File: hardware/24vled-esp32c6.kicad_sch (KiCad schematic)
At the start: 19 parts, among them J1 2601-1106, J3 Barrel_Jack, Q1 AO3400A, Q2 AO3400A, Q3 AO3400A, Q4 AO3400A, Q5 AO3400A, U1 R-78E5.0-1.0

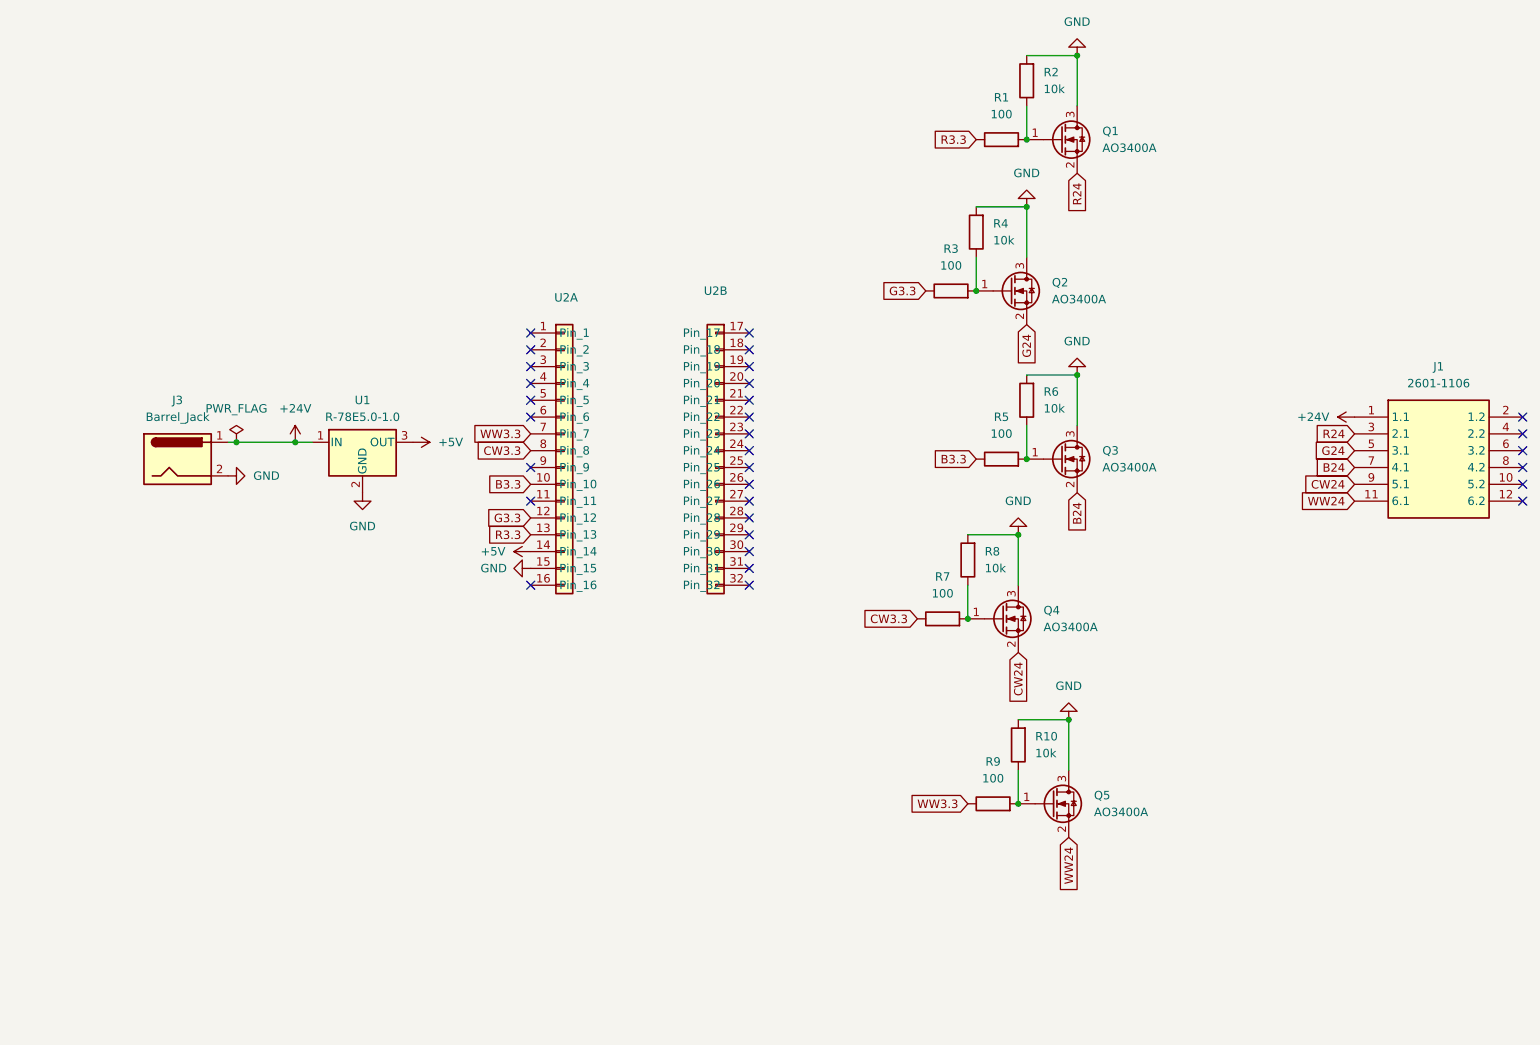
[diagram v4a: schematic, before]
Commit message: add the large cap and remove the flyback diodes
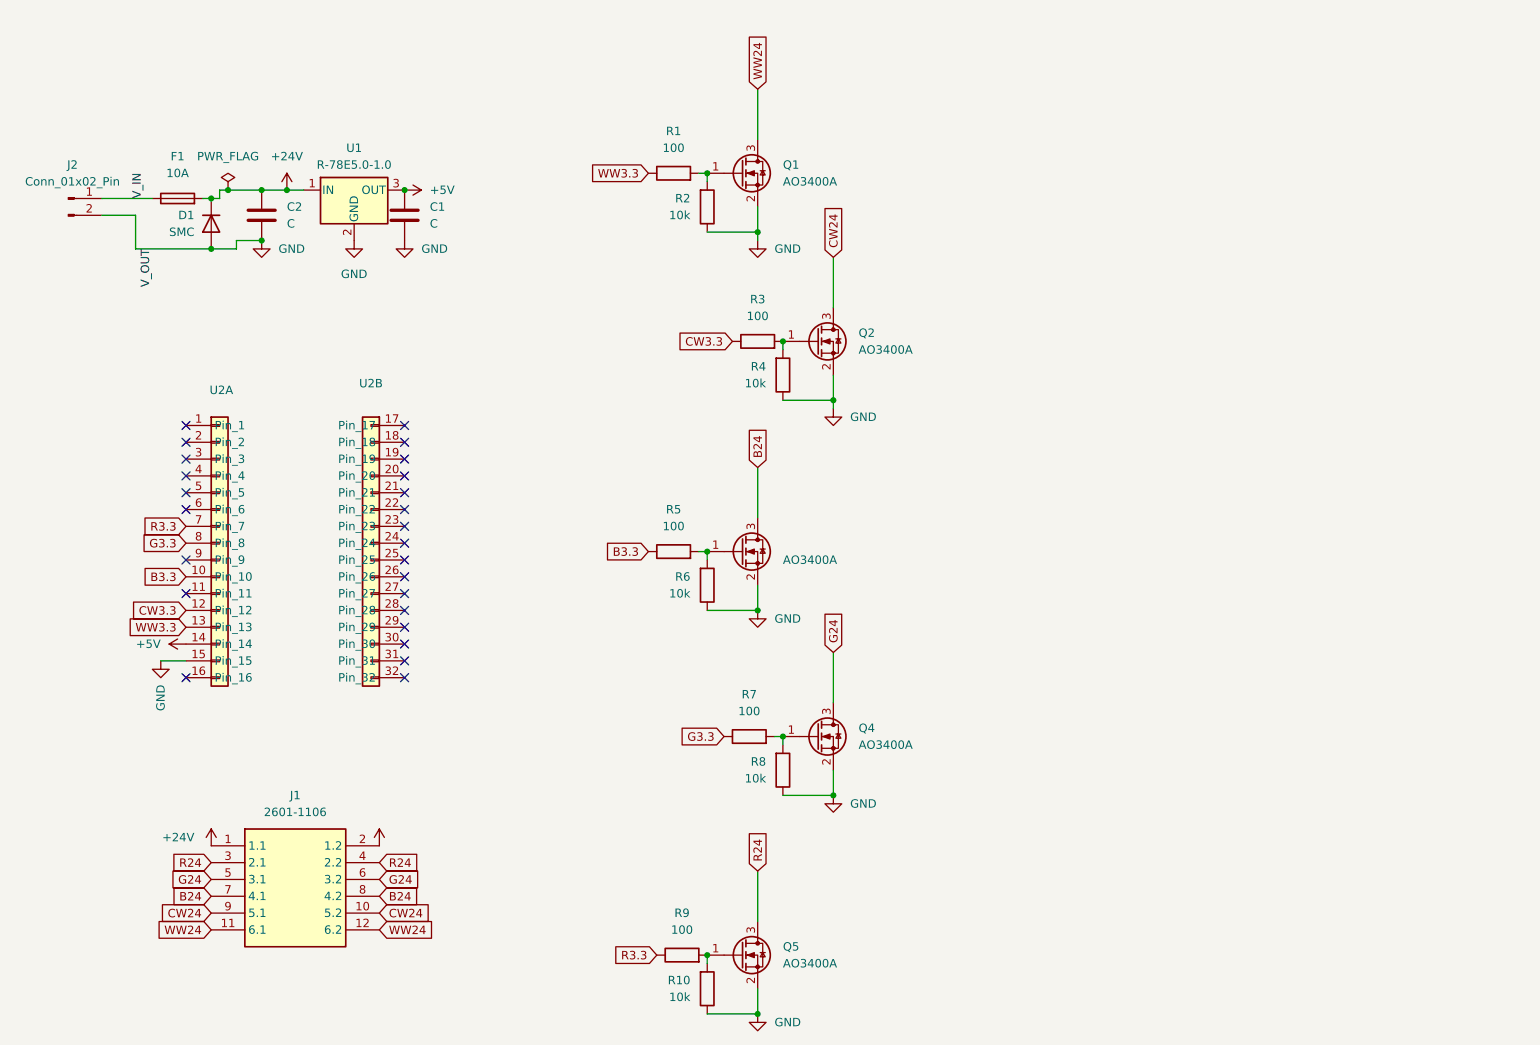
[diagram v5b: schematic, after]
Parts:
- removed J3: Barrel_Jack, Connector_BarrelJack:BarrelJack_CUI_PJ-063AH_Horizontal, symbol Connector:Barrel_Jack
- added C1, C2: C, Capacitor_SMD:C_1206_3216Metric, symbol Device:C
- added D1: SMC, Diode_SMD:D_SMC, symbol Device:D
- added F1: 10A, Fuse:Fuse_Blade_Mini_directSolder, symbol Device:Fuse
- added J2: Conn_01x02_Pin, Connector_AMASS:AMASS_XT30U-M_1x02_P5.0mm_Vertical, symbol Connector:Conn_01x02_Pin
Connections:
- net +24V: now also J1.2 (1.2), C2.1, D1.1 (K), F1.2
- net +5V: now also C1.1
- net B24: now also J1.8 (4.2), Q3.3 (D); no longer Q3.2 (S)
- net CW24: now also J1.10 (5.2), Q2.3 (D); no longer Q4.2 (S)
- net CW3.3: now also R3.1, U2.12 (Pin_12); no longer R7.1, U2.8 (Pin_8)
- net G24: now also J1.6 (3.2), Q4.3 (D); no longer Q2.2 (S)
- net G3.3: now also R7.1, U2.8 (Pin_8); no longer R3.1, U2.12 (Pin_12)
- net GND: now also Q1.2 (S), Q2.2 (S), Q3.2 (S), Q4.2 (S), Q5.2 (S), R10.1, R2.1, R4.1, R6.1, R8.1, C1.2, C2.2, D1.2 (A), J2.2 (Pin_2); no longer Q1.3 (D), Q2.3 (D), Q3.3 (D), Q4.3 (D), Q5.3 (D), R10.2, R2.2, R4.2, R6.2, R8.2
- net R24: now also J1.4 (2.2), Q5.3 (D); no longer Q1.2 (S)
- net R3.3: now also R9.1, U2.7 (Pin_7); no longer R1.1, U2.13 (Pin_13)
- net WW24: now also J1.12 (6.2), Q1.3 (D); no longer Q5.2 (S)
- net WW3.3: now also R1.1, U2.13 (Pin_13); no longer R9.1, U2.7 (Pin_7)
- net at Q2.1 (G), R3.2: now also R4.2; no longer R4.1
- net at Q3.1 (G), R5.2: now also R6.2; no longer R6.1
- net at Q5.1 (G), R9.2: now also R10.2; no longer R10.1
- net at Q1.1 (G), R1.2: now also R2.2; no longer R2.1
- net at Q4.1 (G), R7.2: now also R8.2; no longer R8.1
- new net V_IN: F1.1, J2.1 (Pin_1)
- no-connect marks 31 -> 25
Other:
- moved on the sheet: J1, Q1, Q2, Q4, Q5, R1, R10, R2, R3, R4, R5, R6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

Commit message: final version!
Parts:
- added C3: CP, Capacitor_THT:CP_Radial_D8.0mm_P5.00mm, symbol Device:C
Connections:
- net +24V: now also C3.1
- net GND: now also C3.2
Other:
- moved on the sheet: C1, C2, D1, F1, U1

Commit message: fix warnings and add part numbers
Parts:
- C1, C2: LCSC (none) -> C13585
- D1: LCSC (none) -> C22452
- U1: symbol Regulator_Switching:R-78E5.0-1.0 -> Converter_DCDC:R-78E5.0-1.0
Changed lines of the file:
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@@
 	)
 	(symbol
-		(lib_id "Regulator_Switching:R-78E5.0-1.0")
+		(lib_id "Converter_DCDC:R-78E5.0-1.0")
 		(at 77.47 50.8 0)
 		(unit 1)
@@
 			)
 		)
+		(property "LCSC" "C22452"
+			(at 49.53 54.61 90)
+			(effects
+				(font
+					(size 1.27 1.27)
+				)
+				(hide yes)
+			)
+		)
 		(pin "2"
 		)
@@
 			)
 		)
+		(property "LCSC" "C13585"
+			(at 63.5 54.61 0)
+			(effects
+				(font
+					(size 1.27 1.27)
+				)
+				(hide yes)
+			)
+		)
 		(pin "1"
 		)
@@
 			(at 86.36 54.61 0)
 			(effects
+				(font
+					(size 1.27 1.27)
+				)
+				(hide yes)
+			)
+		)
+		(property "LCSC" "C13585"
+			(at 86.36 54.61 0)
+			(effects

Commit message: update part number
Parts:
- D1: LCSC C22452 -> C211777
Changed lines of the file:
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@@
 			)
 		)
-		(property "LCSC" "C22452"
+		(property "LCSC" "C211777"
 			(at 49.53 54.61 90)
 			(effects
